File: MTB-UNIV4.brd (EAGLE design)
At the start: 100 x 80 mm, 0 parts

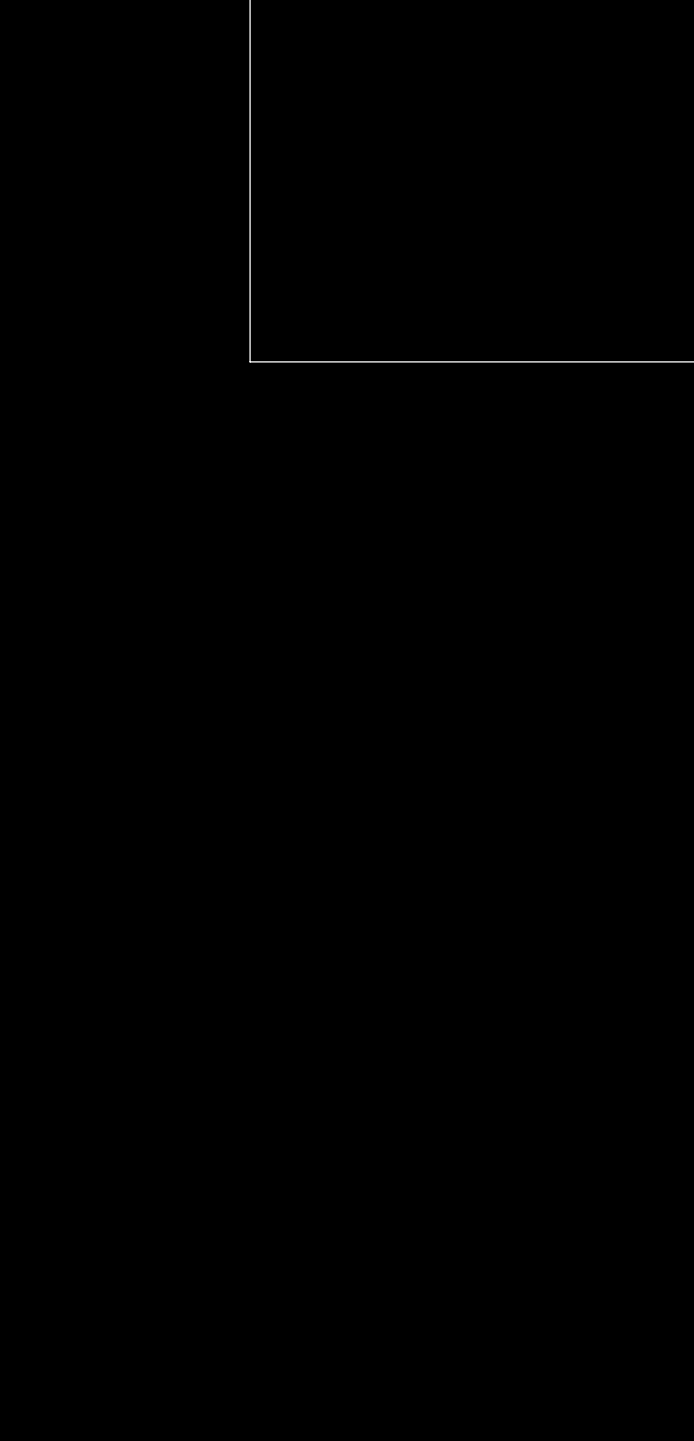
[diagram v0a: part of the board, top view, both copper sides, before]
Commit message: přidány ULN2803A a multiplexery pro digitální IO
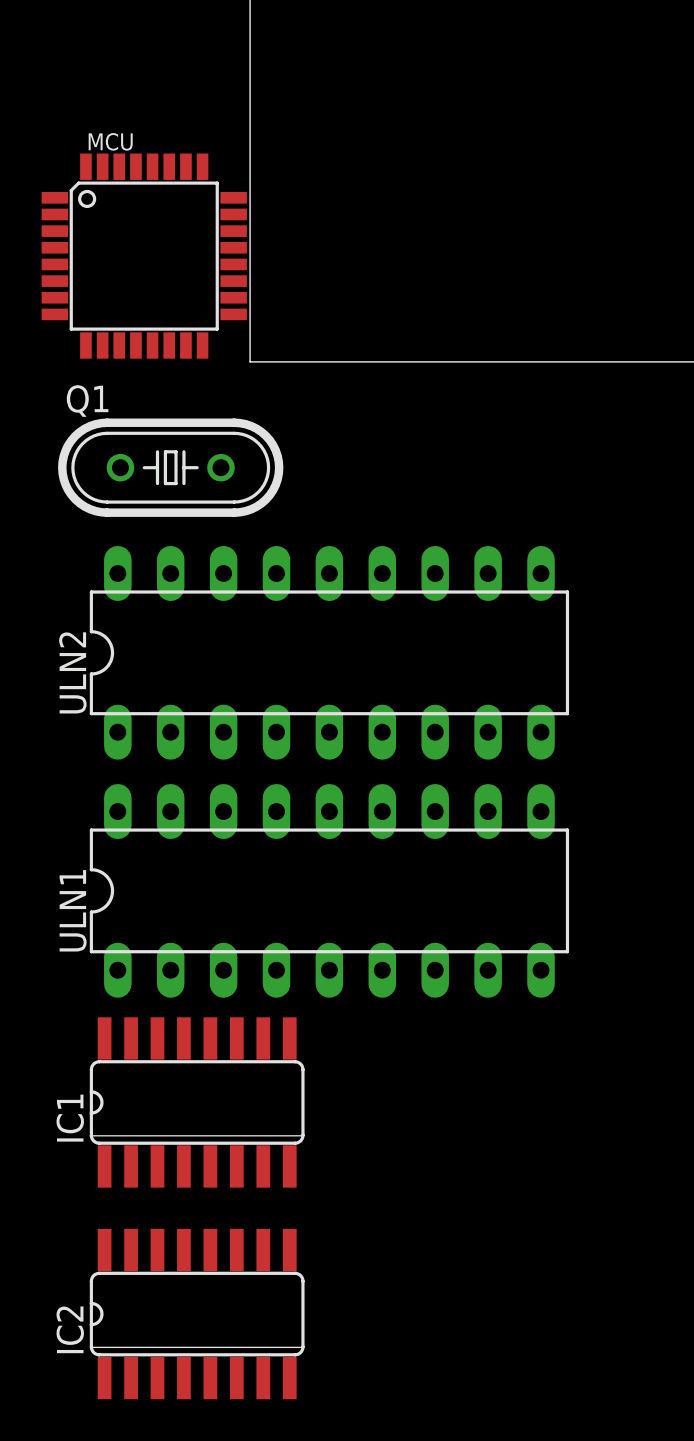
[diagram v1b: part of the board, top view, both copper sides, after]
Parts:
- added IC1, IC2: 4051D, 40xx:SO16
- added MCU: ATMEGA168PA-AU, atmel:TQFP32-08
- added Q1: (no value), crystal:HC49/S
- added ULN1, ULN2: ULN2803A, uln-udn:DIL18
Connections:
- new net AVCC: MCU.18
- new net GND: IC1.8, IC2.8, MCU.21, MCU.3, MCU.5, ULN1.10, ULN1.9, ULN2.10, ULN2.9
- new net VCC: IC1.16, IC2.16, MCU.4, MCU.6
- new net VEE: IC1.7, IC2.7
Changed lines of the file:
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@@
 </autorouter>
 <elements>
+<element name="MCU" library="atmel" library_urn="urn:adsk.eagle:library:105" package="TQFP32-08" package3d_urn="urn:adsk.eagle:package:4313/2" value="ATMEGA168PA-AU" x="-5.08" y="5.08" smashed="yes">
+<attribute name="MF" value="" x="-5.08" y="5.08" size="1.778" layer="27" display="off"/>
+<attribute name="MPN" value="ATMEGA8-16AU" x="-5.08" y="5.08" size="1.778" layer="27" display="off"/>
+<attribute name="NAME" x="-7.8486" y="10.16" size="0.8128" layer="25"/>
+<attribute name="OC_FARNELL" value="9171371" x="-5.08" y="5.08" size="1.778" layer="27" display="off"/>
+<attribute name="OC_NEWARK" value="73M8863" x="-5.08" y="5.08" size="1.778" layer="27" display="off"/>
+<attribute name="POPULARITY" value="11" x="-5.08" y="5.08" size="1.778" layer="27" display="off"/>
+<attribute name="VALUE" x="-8.1026" y="3.81" size="0.8128" layer="27"/>
+</element>
+<element name="Q1" library="crystal" library_urn="urn:adsk.eagle:library:204" package="HC49/S" package3d_urn="urn:adsk.eagle:package:12071/1" value="" x="-3.81" y="-5.08" smashed="yes">
+<attribute name="MF" value="" x="-3.81" y="-5.08" size="1.778" layer="27" display="off"/>
+<attribute name="MPN" value="" x="-3.81" y="-5.08" size="1.778" layer="27" display="off"/>
+<attribute name="NAME" x="-8.89" y="-2.413" size="1.27" layer="25" ratio="10"/>
+<attribute name="OC_FARNELL" value="1667008" x="-3.81" y="-5.08" size="1.778" layer="27" display="off"/>
+<attribute name="OC_NEWARK" value="unknown" x="-3.81" y="-5.08" size="1.778" layer="27" display="off"/>
+<attribute name="POPULARITY" value="49" x="-3.81" y="-5.08" size="1.778" layer="27" display="off"/>
+<attribute name="VALUE" x="-8.89" y="-9.017" size="1.27" layer="27" ratio="10"/>
+</element>
+<element name="ULN2" library="uln-udn" library_urn="urn:adsk.eagle:library:407" package="DIL18" package3d_urn="urn:adsk.eagle:package:16424/2" value="ULN2803A" x="3.81" y="-13.97" smashed="yes">
+<attribute name="NAME" x="-7.874" y="-17.018" size="1.27" layer="25" ratio="10" rot="R90"/>
+<attribute name="POPULARITY" value="5" x="3.81" y="-13.97" size="1.778" layer="27" display="off"/>
+<attribute name="VALUE" x="-5.715" y="-14.605" size="1.27" layer="27" ratio="10"/>
+</element>
+<element name="ULN1" library="uln-udn" library_urn="urn:adsk.eagle:library:407" package="DIL18" package3d_urn="urn:adsk.eagle:package:16424/2" value="ULN2803A" x="3.81" y="-25.4" smashed="yes">
+<attribute name="NAME" x="-7.874" y="-28.448" size="1.27" layer="25" ratio="10" rot="R90"/>
+<attribute name="POPULARITY" value="5" x="3.81" y="-25.4" size="1.778" layer="27" display="off"/>
+<attribute name="VALUE" x="-5.715" y="-26.035" size="1.27" layer="27" ratio="10"/>
+</element>
+<element name="IC1" library="40xx" library_urn="urn:adsk.eagle:library:80" package="SO16" package3d_urn="urn:adsk.eagle:package:821/2" value="4051D" x="-2.54" y="-35.56" smashed="yes">
+<attribute name="NAME" x="-8.001" y="-37.592" size="1.27" layer="25" ratio="10" rot="R90"/>
+<attribute name="POPULARITY" value="5" x="-2.54" y="-35.56" size="1.778" layer="27" display="off"/>
+<attribute name="VALUE" x="-6.604" y="-36.195" size="1.27" layer="27" ratio="10"/>
+</element>
+<element name="IC2" library="40xx" library_urn="urn:adsk.eagle:library:80" package="SO16" package3d_urn="urn:adsk.eagle:package:821/2" value="4051D" x="-2.54" y="-45.72" smashed="yes">
+<attribute name="NAME" x="-8.001" y="-47.752" size="1.27" layer="25" ratio="10" rot="R90"/>
+<attribute name="POPULARITY" value="5" x="-2.54" y="-45.72" size="1.778" layer="27" display="off"/>
+<attribute name="VALUE" x="-6.604" y="-46.355" size="1.27" layer="27" ratio="10"/>
+</element>
 </elements>
 <signals>
+<signal name="GND">
+<contactref element="MCU" pad="3"/>
+<contactref element="MCU" pad="5"/>
+<contactref element="MCU" pad="21"/>
+<contactref element="ULN1" pad="9"/>
+<contactref element="ULN1" pad="10"/>
+<contactref element="ULN2" pad="9"/>
+<contactref element="ULN2" pad="10"/>
+<contactref element="IC1" pad="8"/>
+<contactref element="IC2" pad="8"/>
+<wire x1="1.905" y1="-38.6334" x2="1.905" y2="-48.7934" width="0" layer="19" extent="1-1"/>
+<wire x1="13.97" y1="-29.21" x2="1.905" y2="-38.6334" width="0" layer="19" extent="1-1"/>
+<wire x1="13.97" y1="-21.59" x2="13.97" y2="-29.21" width="0" layer="19" extent="1-1"/>
+<wire x1="13.97" y1="-17.78" x2="13.97" y2="-21.59" width="0" layer="19" extent="1-1"/>
+<wire x1="13.97" y1="-10.16" x2="13.97" y2="-17.78" width="0" layer="19" extent="1-1"/>
+<wire x1="-0.7874" y1="5.48" x2="13.97" y2="-10.16" width="0" layer="19" extent="1-1"/>
+<wire x1="-9.3726" y1="4.68" x2="-0.7874" y2="5.48" width="0" layer="19" extent="1-1"/>
+<wire x1="-9.3726" y1="6.28" x2="-9.3726" y2="4.68" width="0" layer="19" extent="1-1"/>
+</signal>
+<signal name="VCC">
+<contactref element="MCU" pad="4"/>
+<contactref element="MCU" pad="6"/>
+<contactref element="IC1" pad="16"/>
+<contactref element="IC2" pad="16"/>
+<wire x1="-6.985" y1="-32.4866" x2="-6.985" y2="-42.6466" width="0" layer="19" extent="1-1"/>
+<wire x1="-9.3726" y1="3.88" x2="-6.985" y2="-32.4866" width="0" layer="19" extent="1-1"/>
+<wire x1="-9.3726" y1="5.48" x2="-9.3726" y2="3.88" width="0" layer="19" extent="1-1"/>
+</signal>
+<signal name="AVCC">
+<contactref element="MCU" pad="18"/>
+</signal>
+<signal name="VEE">
+<contactref element="IC1" pad="7"/>
+<contactref element="IC2" pad="7"/>
+<wire x1="0.635" y1="-38.6334" x2="0.635" y2="-48.7934" width="0" layer="19" extent="1-1"/>
+</signal>
 </signals>
 <mfgpreviewcolors>
@@
 </board>
 </drawing>
+<compatibility>
+<note version="8.2" severity="warning">
+Since Version 8.2, EAGLE supports online libraries. The ids
+of those online libraries will not be understood (or retained)
+with this version.
+</note>
+<note version="8.3" severity="warning">
+Since Version 8.3, EAGLE supports URNs for individual library
+assets (packages, symbols, and devices). The URNs of those assets
+will not be understood (or retained) with this version.
+</note>
+<note version="8.3" severity="warning">
+Since Version 8.3, EAGLE supports the association of 3D packages
+with devices in libraries, schematics, and board files. Those 3D
+packages will not be understood (or retained) with this version.
+</note>
+</compatibility>
 </eagle>

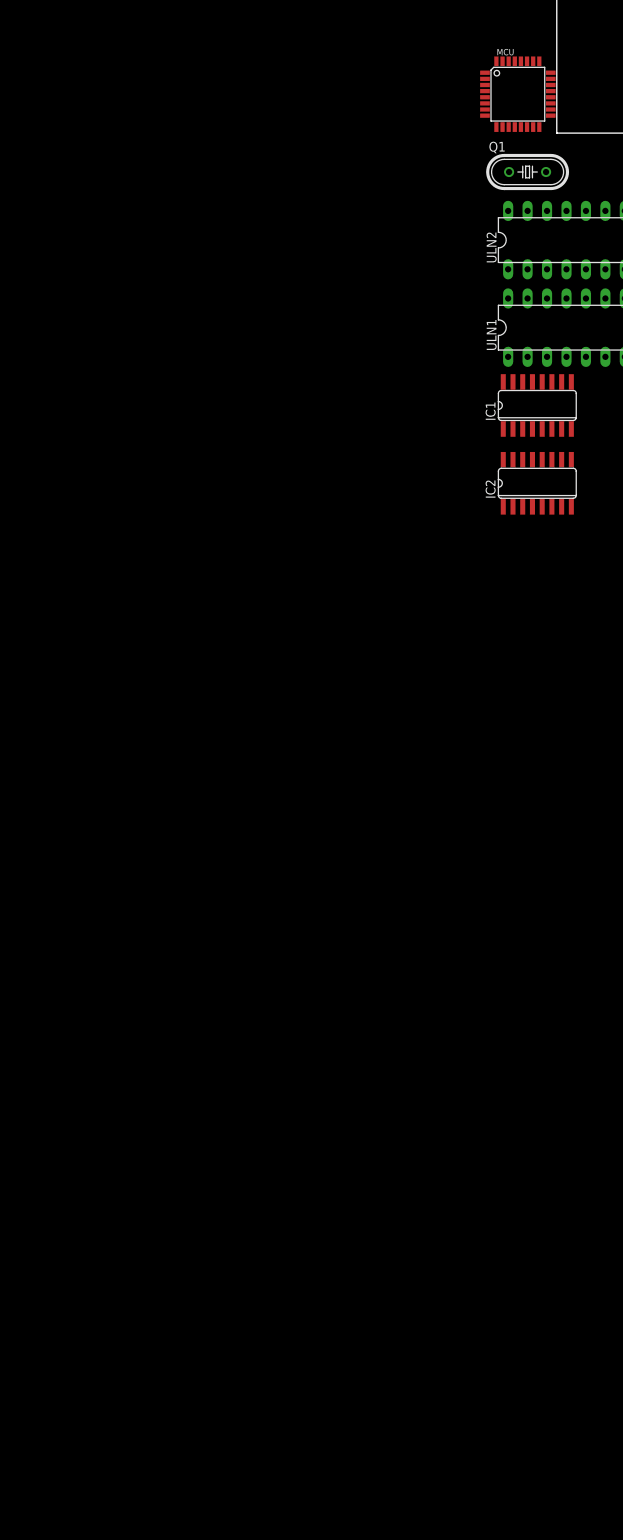
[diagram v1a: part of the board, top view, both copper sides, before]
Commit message: Prototyp 1, chybí svorkovnice vstupů a výstupů, selektor adresy a indikační led diody. Možná dodělat ochranu výstupů, ale kdyžtak shoří ULN.
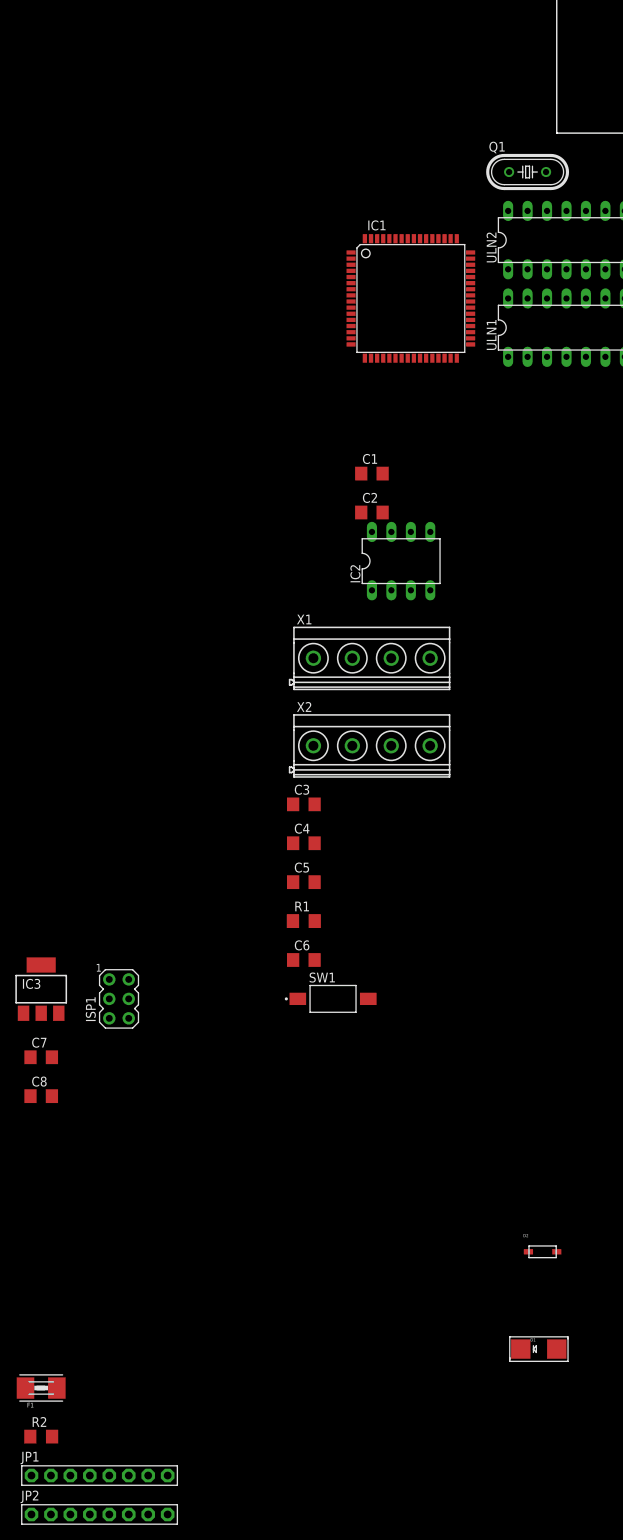
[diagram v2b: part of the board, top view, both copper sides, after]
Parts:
- removed MCU: ATMEGA168PA-AU, atmel:TQFP32-08
- added C1, C2, C3, C4, C5, C6, C7, C8: (no value), rcl:C1206
- added D1: Schottky, adafruit:SMADIODE
- added D2: Zener, adafruit:SOD-123
- added F1: (no value), adafruit:1812
- added IC3: NCP1117, ElectroKrt:SOT223
- added ISP1: AVRISP-6, adafruit:AVRISP
- added JP1, JP2: (no value), adafruit:1X08-BIG
- added R1, R2: (no value), rcl:R1206
- added SW1: FSMSM, Switch:FSMSM
- added X1, X2: MKDSN1,5/4-5,08, con-phoenix-508:MKDSN1,5/4-5,08
- IC1: value 4051D -> MEGA128-A; device 40xx:SO16 -> atmel:TQFP64
- IC2: value 4051D -> SN75176AP; device 40xx:SO16 -> ic-package:DIL08
- moved IC1 21.6 mm to (-19.1, -21.6)
- moved IC2 20.5 mm to (-20.3, -55.9)
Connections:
- removed net AVCC: MCU.18
- removed net VCC: IC1.16, IC2.16, MCU.4, MCU.6
- removed net VEE: IC1.7, IC2.7
- new net +12V: X1.1, X2.1
- new net +5V: C3.1, C4.1, C5.1, C8.1, IC1.21, IC1.52, IC1.64, IC2.8, IC3.2, IC3.4, ISP1.2, R1.2
- new net D-IN(A)1: IC1.51
- new net D-IN(A)2: IC1.50
- new net D-IN(A)3: IC1.49
- new net D-IN(A)4: IC1.48
- new net D-IN(A)5: IC1.47
- new net D-IN(A)6: IC1.46
- new net D-IN(A)7: IC1.45
- new net D-IN(A)8: IC1.44
- new net D-IN(B)1: IC1.35
- new net D-IN(B)2: IC1.36
- new net D-IN(B)3: IC1.37
- new net D-IN(B)4: IC1.38
- new net D-IN(B)5: IC1.39
- new net D-IN(B)6: IC1.40
- new net D-IN(B)7: IC1.41
- new net D-IN(B)8: IC1.42
- new net D-OUT(A)1: IC1.25, ULN1.1
- new net D-OUT(A)2: IC1.26, ULN1.2
- new net D-OUT(A)3: IC1.27, ULN1.3
- new net D-OUT(A)4: IC1.28, ULN1.4
- new net D-OUT(A)5: IC1.29, ULN1.5
- new net D-OUT(A)6: IC1.30, ULN1.6
- new net D-OUT(A)7: IC1.31, ULN1.7
- new net D-OUT(A)8: IC1.32, ULN1.8
- new net D-OUT(B)1: IC1.61, ULN2.1
- new net D-OUT(B)2: IC1.60, ULN2.2
- new net D-OUT(B)3: IC1.59, ULN2.3
- new net D-OUT(B)4: IC1.58, ULN2.4
- new net D-OUT(B)5: IC1.57, ULN2.5
- new net D-OUT(B)6: IC1.56, ULN2.6
- new net D-OUT(B)7: IC1.55, ULN2.7
- new net D-OUT(B)8: IC1.54, ULN2.8
- new net MISO: IC1.13, ISP1.1
- new net MOSI: IC1.12, ISP1.4
- new net N$1: C2.1, IC1.24, Q1.2
- new net N$10: JP1.1, ULN1.18
- new net N$11: JP2.8, ULN2.11
- new net N$12: JP2.7, ULN2.12
- new net N$13: C7.1, D1.C, IC3.3
- new net N$14: D1.A, D2.C, F1.2
- new net N$15: JP2.6, ULN2.13
- new net N$16: JP2.5, ULN2.14
- new net N$17: JP2.4, ULN2.15
- new net N$18: JP2.3, ULN2.16
- new net N$19: JP2.2, ULN2.17
- new net N$2: JP1.8, ULN1.11
- new net N$20: JP2.1, ULN2.18
- new net N$3: C1.1, IC1.23, Q1.1
- new net N$4: JP1.7, ULN1.12
- new net N$5: JP1.6, ULN1.13
- new net N$6: JP1.5, ULN1.14
- new net N$7: JP1.4, ULN1.15
- new net N$8: JP1.3, ULN1.16
- new net N$9: JP1.2, ULN1.17
- new net RS-A: IC2.6, R2.1, X1.2, X2.2
- new net RS-B: IC2.7, R2.2, X1.3, X2.3
- new net RS-D: IC1.3, IC2.4
- new net RS-E: IC1.4, IC2.2, IC2.3
- new net RS-R: IC1.2, IC2.1
- new net RST: C6.1, IC1.20, ISP1.5, R1.1, SW1.2
- new net SCK: IC1.11, ISP1.3
- new net V+: F1.1
- net GND: now also C1.2, C2.2, C3.2, C4.2, C5.2, C6.2, C7.2, C8.2, D2.A, IC1.22, IC1.53, IC1.63, IC2.5, IC3.1, ISP1.6, SW1.1, X1.4, X2.4; no longer IC1.8, IC2.8, MCU.21, MCU.3, MCU.5
